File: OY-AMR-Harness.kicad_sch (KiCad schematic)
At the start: 0 parts

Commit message: Added component library
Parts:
- added SW1: 89165-01, symbol OYAMR_Library:89165-01
- added U1: OY-AMR 12V Control Board, https://github.com/elfremdrift/OY-AMR-12V, symbol OYAMR_Library:Control_Board
- added U2: ~, symbol OYAMR_Library:Curtis_1239E_1

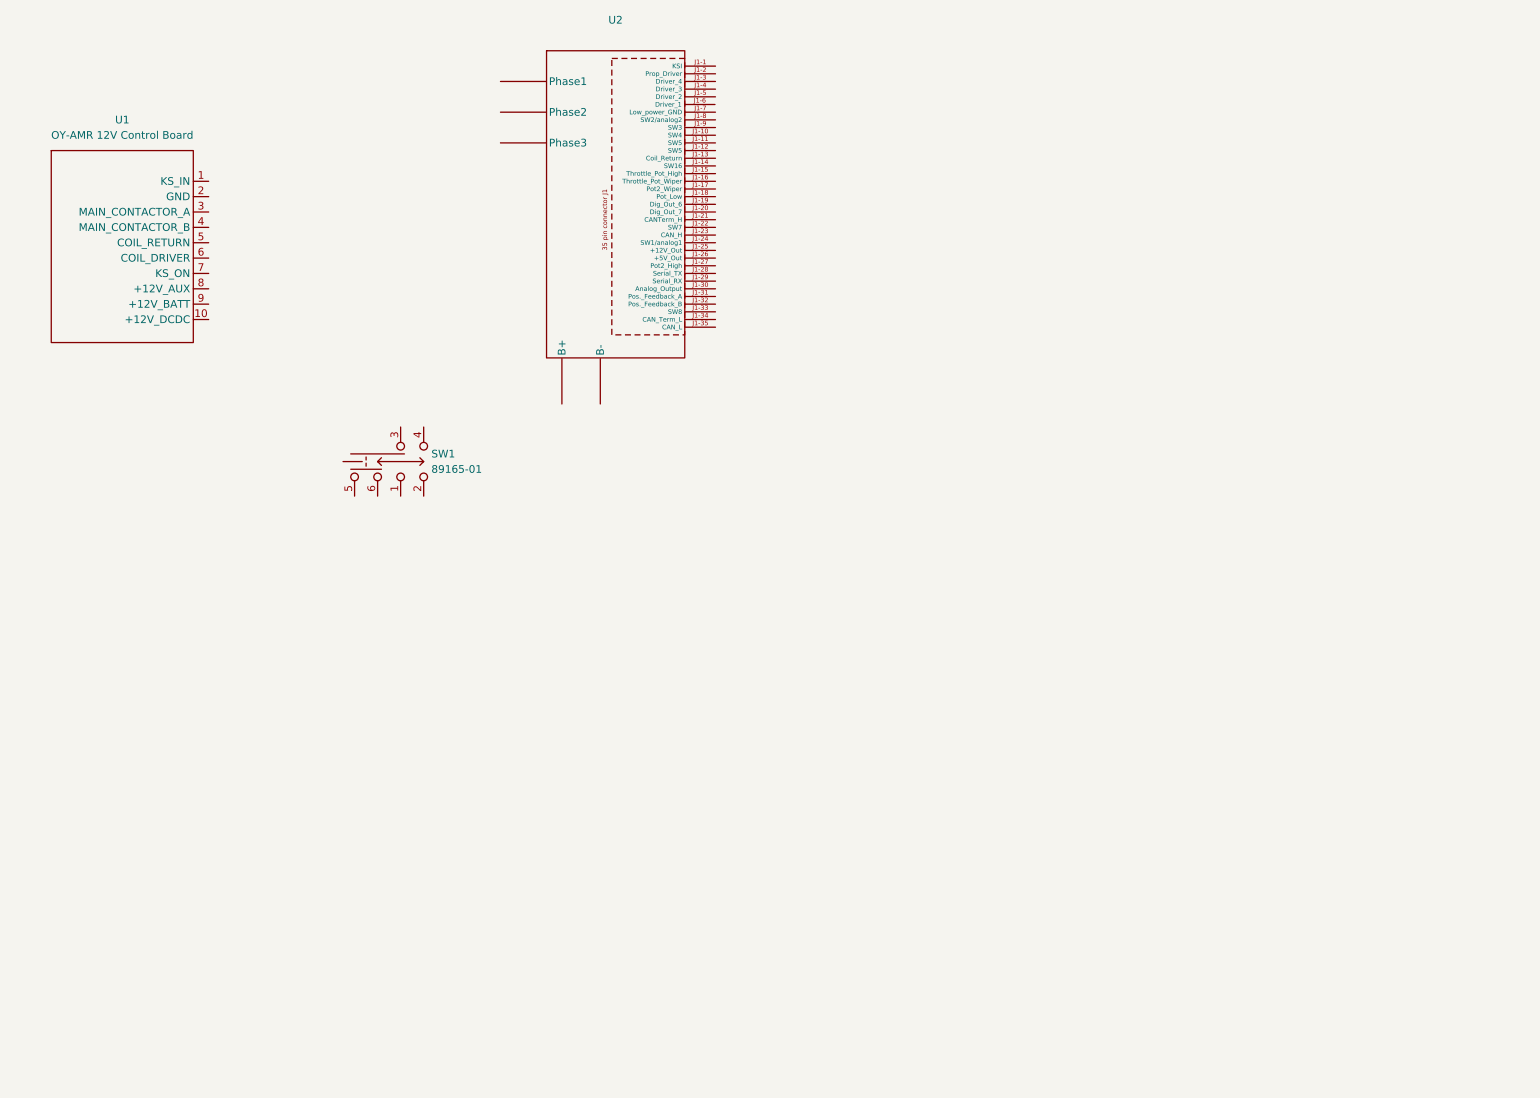
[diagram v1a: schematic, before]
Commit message: Main parts of motor control harness
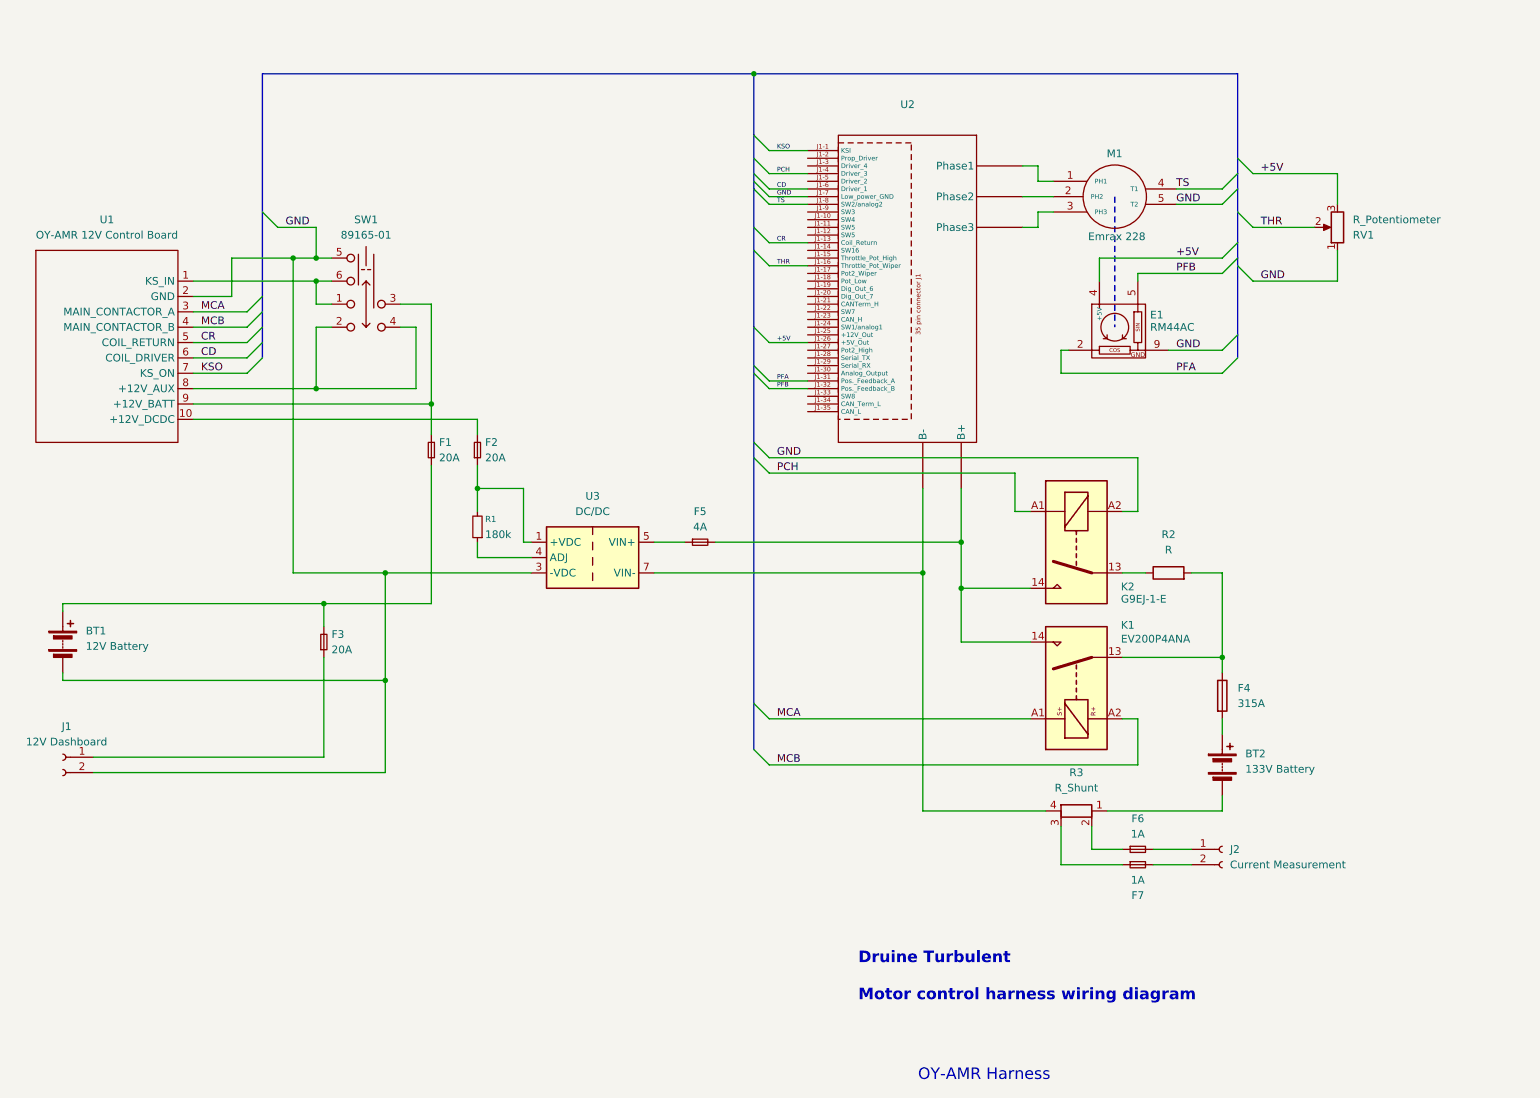
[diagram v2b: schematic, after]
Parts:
- added BT1: 12V Battery, symbol Device:Battery
- added BT2: 133V Battery, symbol Device:Battery
- added E1: RM44AC, symbol OYAMR_Library:RLS RM44AC encoder
- added F1, F2, F3: 20A, symbol Device:Fuse_Small
- added F4: 315A, symbol Device:Fuse
- added F5: 4A, symbol Device:Fuse_Small
- added F6, F7: 1A, symbol Device:Fuse_Small
- added J1: 12V Dashboard, symbol Connector:Conn_01x02_Socket
- added J2: Current Measurement, symbol Connector:Conn_01x02_Socket
- added K1: EV200P4ANA, Relay_THT:Relay_SPST_Panasonic_ADW11, symbol Relay:ADW11
- added K2: G9EJ-1-E, Relay_THT:Relay_SPST-NO_Fujitsu_FTR-LYAA005x_FormA_Vertical, symbol Relay:Fujitsu_FTR-LYAA005x
- added M1: Emrax 228, symbol OYAMR_Library:3_Phase_Motor
- added R1: 180k, symbol Device:R_Small
- added R2: R, symbol Device:R
- added R3: R_Shunt, symbol Device:R_Shunt
- added RV1: R_Potentiometer, symbol Device:R_Potentiometer
- added U3: DC/DC, Converter_DCDC:Converter_DCDC_Silvertel_Ag99xxLP_THT, symbol Converter_DCDC:Ag9905LP
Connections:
- net at U2. (B-): now also M1.3 (PH3)
- net KSO: now reaches U2.J1-1 (KSI)
- net KSO: now also U1.7 (KS_ON)
- net CR: now reaches U2.J1-13 (Coil_Return)
- net CR: now also U1.5 (COIL_RETURN)
- net THR: now reaches U2.J1-16 (Throttle_Pot_Wiper)
- net THR: now also RV1.2
- net +5V: now reaches U2.J1-26 (+5V_Out)
- net +5V: now also E1.4 (+5V), RV1.3
- net PFA: now reaches U2.J1-31 (Pos._Feedback_A)
- net PFA: now also E1.2
- net PFB: now reaches U2.J1-32 (Pos._Feedback_B)
- net PFB: now also E1.5
- net PCH: now reaches U2.J1-4 (Driver_3)
- net PCH: now also K2.A1
- net CD: now reaches U2.J1-6 (Driver_1)
- net CD: now also U1.6 (COIL_DRIVER)
- net GND: now reaches U2.J1-7 (Low_power_GND)
- net GND: now also SW1.5 (E), U1.2 (GND), BT1.2 (-), E1.9, J1.2 (Pin_2), K2.A2, M1.5 (T2), RV1.1, U3.3 (-VDC)
- net TS: now reaches U2.J1-8 (SW2/analog2)
- net TS: now also M1.4 (T1)
- net at SW1.1 (A): now also SW1.6 (F), U1.1 (KS_IN)
- net at SW1.2 (B): now also SW1.4 (D), U1.8 (+12V_AUX)
- net at SW1.3 (C): now also U1.9 (+12V_BATT), F1.1
- net at U1.10 (+12V_DCDC): now also F2.2
- net MCA: now reaches U1.3 (MAIN_CONTACTOR_A)
- net MCA: now also K1.A1
- net MCB: now reaches U1.4 (MAIN_CONTACTOR_B)
- net MCB: now also K1.A2
- new net: BT2.1 (+), F4.2
- new net: BT2.2 (-), R3.1
- new net: F2.1, R1.2, U3.1 (+VDC), U3.2 (+VDC)
- new net: R3.4, U2. (B-), U3.7 (VIN-), U3.8 (VIN-)
- new net: F5.2, K1.14, K2.14, U2. (B-)
- new net: M1.1 (PH1), U2. (B-)
- new net: M1.2 (PH2), U2. (B-)
- new net: R1.1, U3.4 (ADJ)
- new net: F5.1, U3.5 (VIN+), U3.6 (VIN+)
- new net: F3.1, J1.1 (Pin_1)
- new net: BT1.1 (+), F1.2, F3.2
- new net: F4.1, K1.13, R2.2
- new net: F7.1, R3.3
- new net: F7.2, J2.2 (Pin_2)
- new net: F6.2, J2.1 (Pin_1)
- new net: K2.13, R2.1
- new net: F6.1, R3.2
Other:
- note added: "Druine Turbulent Motor control harness wiring diagram"
- note added: "OY-AMR Harness"
- moved on the sheet: SW1, U1, U2

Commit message: Review færdig og diagram rettet i samarbejde med Søren
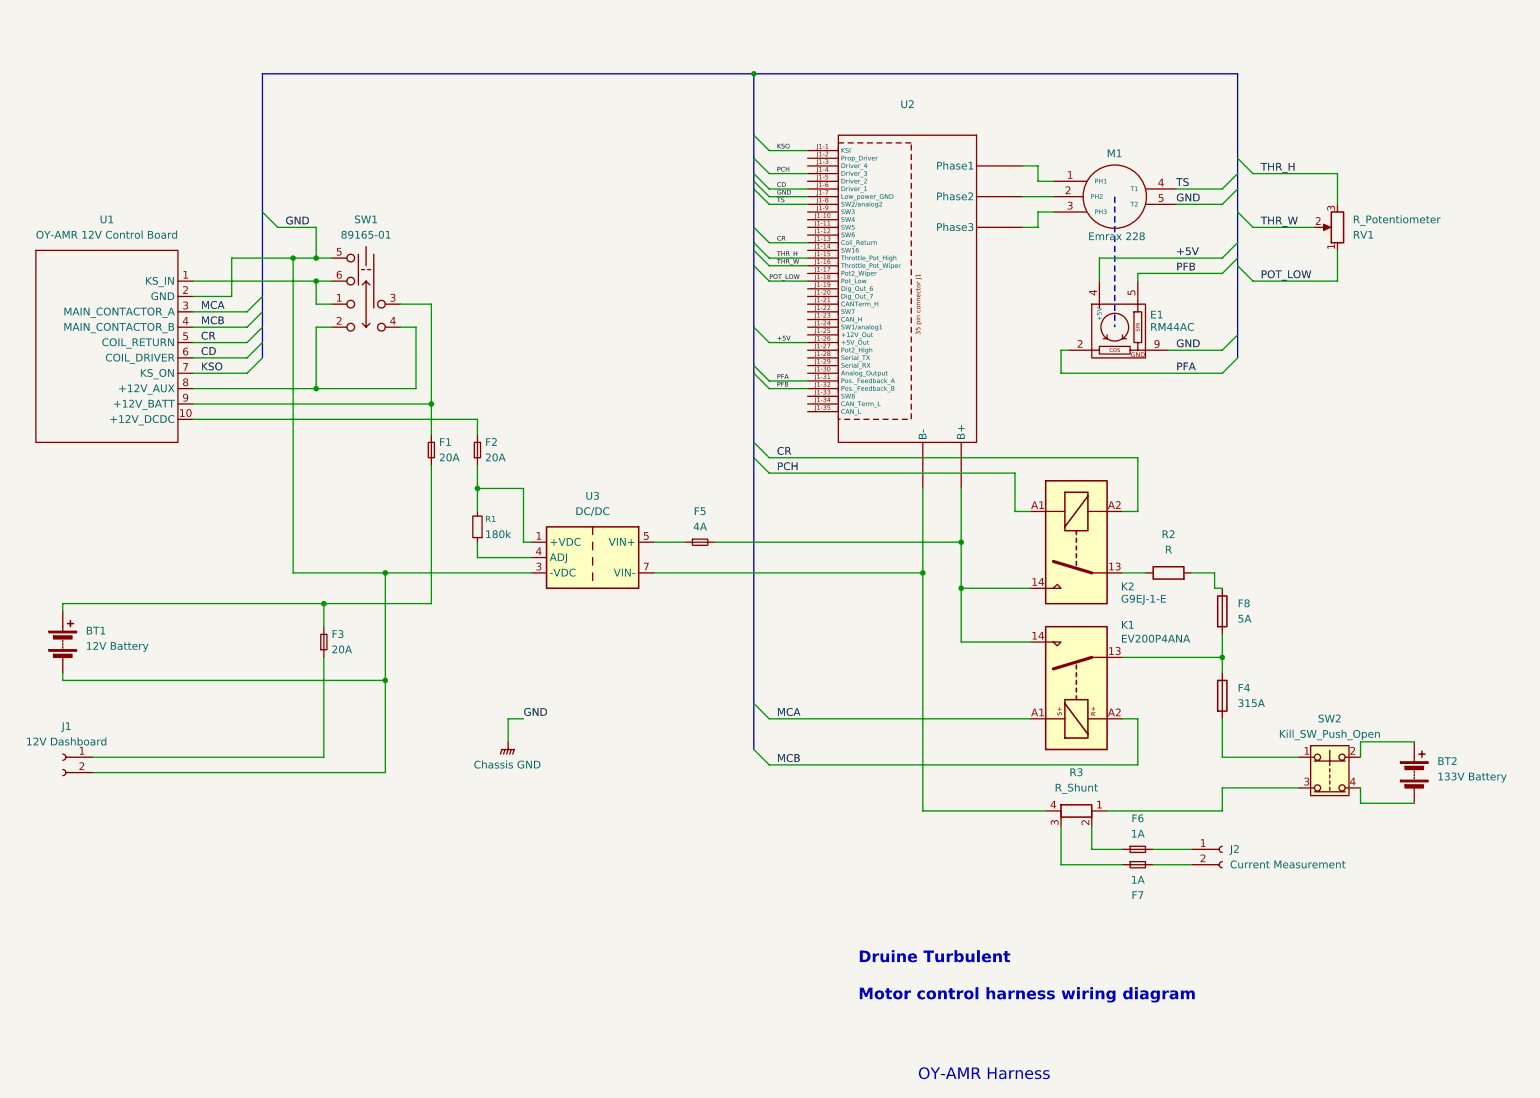
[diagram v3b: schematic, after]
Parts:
- added F8: 5A, symbol Device:Fuse
- added SW2: Kill_SW_Push_Open, symbol Switch:SW_Push_Open_Dual
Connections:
- net +5V: no longer RV1.3
- net CR: now also K2.A2
- net at F4.2: now also SW2.1; no longer BT2.1 (+)
- net at R3.1: now also SW2.3; no longer BT2.2 (-)
- net THR_H: now reaches U2.J1-15 (Throttle_Pot_High)
- net THR_H: now also RV1.3
- net POT_LOW: now reaches U2.J1-18 (Pot_Low)
- net POT_LOW: now also RV1.1
- net at F4.1, K1.13: now also F8.2; no longer R2.2
- net GND renamed Chassis GND
- net Chassis GND: no longer K2.A2, RV1.1
- net THR renamed THR_W
- new net: BT2.1 (+), SW2.2
- new net: BT2.2 (-), SW2.4
- new net: F8.1, R2.2
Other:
- moved on the sheet: BT2

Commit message: Small fixes
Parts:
- F8: value 5A -> 4A
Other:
- moved on the sheet: F5
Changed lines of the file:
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@@
 	(wire
 		(pts
+			(xy 124.46 132.08) (xy 120.65 132.08)
+		)
+		(stroke
+			(width 0)
+			(type default)
+		)
+	)
+	(wire
+		(pts
 			(xy 88.9 54.61) (xy 85.09 54.61)
 		)
@@
 	(wire
 		(pts
-			(xy 237.49 109.22) (xy 238.76 109.22)
-		)
-		(stroke
-			(width 0)
-			(type default)
-			(color 221 133 0 1)
-		)
-	)
-	(wire
-		(pts
 			(xy 195.58 109.22) (xy 195.58 118.11)
 		)
@@
 	(wire
 		(pts
+			(xy 120.65 132.08) (xy 120.65 134.62)
+		)
+		(stroke
+			(width 0)
+			(type default)
+		)
+	)
+	(wire
+		(pts
 			(xy 163.83 90.17) (xy 204.47 90.17)
 		)
@@
 	(wire
 		(pts
-			(xy 144.78 101.6) (xy 149.86 101.6)
+			(xy 144.78 101.6) (xy 181.61 101.6)
 		)
 		(stroke
@@
 	(wire
 		(pts
-			(xy 251.46 137.16) (xy 238.76 137.16)
+			(xy 238.76 106.68) (xy 238.76 109.22)
 		)
 		(stroke
 			(width 0)
 			(type default)
+			(color 221 133 0 1)
 		)
 	)
 	(wire
 		(pts
-			(xy 68.58 71.12) (xy 77.47 71.12)
+			(xy 251.46 137.16) (xy 238.76 137.16)
 		)
 		(stroke
@@
 		)
 	)
-	(bus
+	(wire
 		(pts
-			(xy 161.29 38.1) (xy 161.29 40.64)
+			(xy 68.58 71.12) (xy 77.47 71.12)
 		)
 		(stroke
@@
 	(bus
 		(pts
-			(xy 241.3 38.1) (xy 241.3 40.64)
+			(xy 161.29 38.1) (xy 161.29 40.64)
 		)
 		(stroke
@@
 		)
 	)
-	(wire
+	(bus
 		(pts
-			(xy 163.83 36.83) (xy 170.18 36.83)
+			(xy 241.3 38.1) (xy 241.3 40.64)
 		)
 		(stroke
@@
 	(wire
 		(pts
-			(xy 120.65 130.81) (xy 123.19 130.81)
+			(xy 163.83 36.83) (xy 170.18 36.83)
 		)
 		(stroke
@@
 	(wire
 		(pts
-			(xy 154.94 101.6) (xy 195.58 101.6)
+			(xy 186.69 101.6) (xy 195.58 101.6)
 		)
 		(stroke
@@
 	(wire
 		(pts
-			(xy 237.49 106.68) (xy 233.68 106.68)
+			(xy 238.76 106.68) (xy 233.68 106.68)
 		)
 		(stroke
@@
 		)
 	)
-	(wire
-		(pts
-			(xy 237.49 109.22) (xy 237.49 106.68)
-		)
-		(stroke
-			(width 0)
-			(type default)
-			(color 221 133 0 1)
-		)
-	)
 	(bus
 		(pts
@@
 	(wire
 		(pts
-			(xy 120.65 134.62) (xy 120.65 130.81)
-		)
-		(stroke
-			(width 0)
-			(type default)
-		)
-	)
-	(wire
-		(pts
 			(xy 68.58 73.66) (xy 77.47 73.66)
 		)
@@
 	)
 	(label "GND"
-		(at 123.19 130.81 0)
+		(at 124.46 132.08 180)
 		(effects
 			(font
 				(size 1.27 1.27)
 			)
-			(justify left bottom)
+			(justify right bottom)
 		)
 	)
@@
 			)
 		)
-		(property "Value" "5A"
+		(property "Value" "4A"
 			(at 241.3 114.2999 0)
 			(effects
@@
 	(symbol
 		(lib_id "Device:Fuse_Small")
-		(at 152.4 101.6 0)
+		(at 184.15 101.6 0)
 		(unit 1)
 		(exclude_from_sim no)
@@
 		(fields_autoplaced yes)
 		(property "Reference" "F5"
-			(at 152.4 96.52 0)
+			(at 184.15 96.52 0)
 			(effects
 				(font
@@
 		)
 		(property "Value" "4A"
-			(at 152.4 99.06 0)
+			(at 184.15 99.06 0)
 			(effects
 				(font
@@
 		)
 		(property "Footprint" ""
-			(at 152.4 101.6 0)
+			(at 184.15 101.6 0)
 			(effects
 				(font
@@
 		)
 		(property "Datasheet" "~"
-			(at 152.4 101.6 0)
+			(at 184.15 101.6 0)
 			(effects
 				(font
@@
 		)
 		(property "Description" "Fuse, small symbol"
-			(at 152.4 101.6 0)
+			(at 184.15 101.6 0)
 			(effects
 				(font
